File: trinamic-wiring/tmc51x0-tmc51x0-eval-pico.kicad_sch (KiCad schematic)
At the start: 3 parts, among them M1 Stepper_Motor

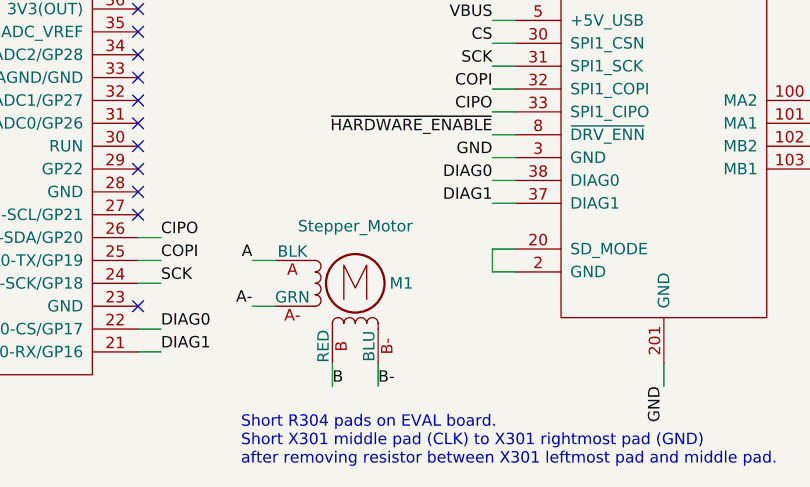
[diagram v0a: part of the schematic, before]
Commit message: Split tmc51x0 into spi and uart
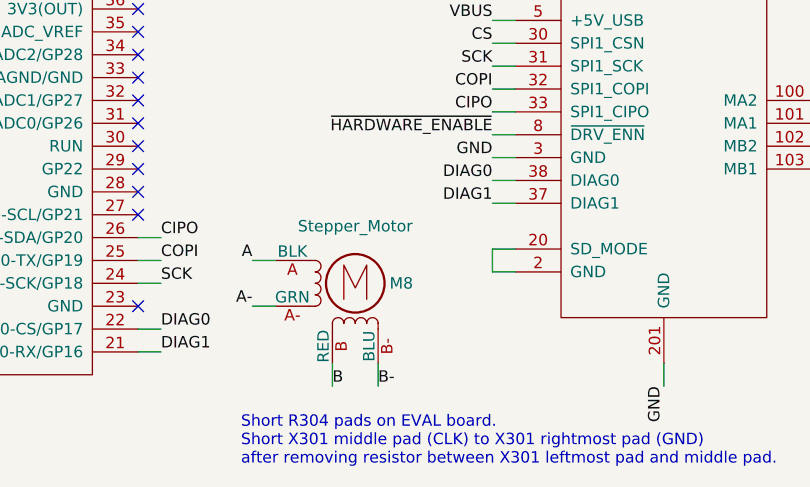
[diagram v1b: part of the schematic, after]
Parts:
- renumbered M1 to M8
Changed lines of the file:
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@@
   (title_block
     (title "Trinamic Wiring")
-    (date "2024-07-31")
+    (date "2024-08-01")
     (rev "0.5")
     (company "Janelia Research Campus")
@@
   (symbol (lib_id "Janelia:Stepper_Motor_QSH2818-32-07-006") (at 147.32 128.27 0) (unit 1)
     (in_bom yes) (on_board yes) (dnp no)
-    (property "Reference" "M1" (at 151.13 128.27 0)
+    (property "Reference" "M8" (at 151.13 128.27 0)
       (effects (font (size 1.27 1.27)) (justify left))
     )
@@
     (instances
       (project "trinamic-wiring"
-        (path "/e4144788-6304-493f-818e-5d881d3b7418/a161638e-a96f-4455-865a-1d7502675f43/b07f1639-ae99-4e69-a4ff-b15d0c967980/dab15df5-b51f-4c1f-8fc9-49b45f8778bf"
-          (reference "M1") (unit 1)
+        (path "/e4144788-6304-493f-818e-5d881d3b7418/a161638e-a96f-4455-865a-1d7502675f43/ca35872a-a0db-401c-97bd-5b4a3f731cf1/a4ac6707-60d1-4489-9732-1d0914f88b38/dab15df5-b51f-4c1f-8fc9-49b45f8778bf"
+          (reference "M8") (unit 1)
         )
       )
@@
     (instances
       (project "trinamic-wiring"
-        (path "/e4144788-6304-493f-818e-5d881d3b7418/a161638e-a96f-4455-865a-1d7502675f43/b07f1639-ae99-4e69-a4ff-b15d0c967980/dab15df5-b51f-4c1f-8fc9-49b45f8778bf"
+        (path "/e4144788-6304-493f-818e-5d881d3b7418/a161638e-a96f-4455-865a-1d7502675f43/ca35872a-a0db-401c-97bd-5b4a3f731cf1/a4ac6707-60d1-4489-9732-1d0914f88b38/dab15df5-b51f-4c1f-8fc9-49b45f8778bf"
           (reference "A3") (unit 1)
         )
@@
     (instances
       (project "trinamic-wiring"
-        (path "/e4144788-6304-493f-818e-5d881d3b7418/a161638e-a96f-4455-865a-1d7502675f43/b07f1639-ae99-4e69-a4ff-b15d0c967980/dab15df5-b51f-4c1f-8fc9-49b45f8778bf"
+        (path "/e4144788-6304-493f-818e-5d881d3b7418/a161638e-a96f-4455-865a-1d7502675f43/ca35872a-a0db-401c-97bd-5b4a3f731cf1/a4ac6707-60d1-4489-9732-1d0914f88b38/dab15df5-b51f-4c1f-8fc9-49b45f8778bf"
           (reference "EVAL1") (unit 1)
         )
